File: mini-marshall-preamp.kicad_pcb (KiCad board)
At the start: 2 copper layers, 44 parts, among them J1 LO, J2 HI, J3 AudioJack2, J4 6V3, J5 370V GND, J6 370V, J7 6V3 GND, U1 6N2P, U2 6N2P

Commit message: Use external connection footprints for pots and jacks
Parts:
- J1: footprint Connector_Audio:Jack_6.35mm_Neutrik_NMJ6HFD2-AU_Horizontal -> Connector_Wire:SolderWire-1sqmm_1x04_P5.4mm_D1.4mm_OD2.7mm
- J2: footprint Connector_Audio:Jack_6.35mm_Neutrik_NMJ6HFD2-AU_Horizontal -> Connector_Wire:SolderWire-1sqmm_1x02_P5.4mm_D1.4mm_OD2.7mm
- J3: value AudioJack2 -> OUT; footprint Connector_Audio:Jack_6.35mm_Neutrik_NMJ6HFD2-AU_Horizontal -> Connector_Wire:SolderWire-1sqmm_1x02_P5.4mm_D1.4mm_OD2.7mm
- RV1, RV2, RV3, RV4, RV5: footprint Potentiometer_THT:Potentiometer_Alps_RK163_Single_Horizontal -> Connector_Wire:SolderWire-1sqmm_1x03_P5.4mm_D1.4mm_OD2.7mm
- moved C9 65.8 mm to (129.9, 118.4), turned to 90 degrees
- moved R11 58.1 mm to (116.3, 112.7), turned to 90 degrees
- moved C5 49.6 mm to (151.8, 102.1), turned to -90 degrees
- moved R4 40.8 mm to (97.7, 112.4), turned to 90 degrees
- moved J2 37.1 mm to (46.0, 102.9)
- moved J1 35.6 mm to (45.9, 85.0), turned to 90 degrees
- moved C4 26.5 mm to (94.2, 117.7), turned to 180 degrees
- moved C3 16.2 mm to (106.0, 99.8), turned to -90 degrees
- turned RV1 to 180 degrees
- turned RV2 to 180 degrees
- turned RV3 to 180 degrees
- turned RV4 to 180 degrees
- turned RV5 to 180 degrees
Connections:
- C2 pad 1: Net-(C2-Pad1) -> Net-(J1-SN)
- C3 pad 1: Net-(C3-Pad1) -> Net-(J1-S)
- R1 pad 1: Net-(J2-PadS) -> Net-(J2-S)
- R2 pad 1: Net-(J2-PadS) -> Net-(J2-S)
- R4 pad 2: Net-(C3-Pad1) -> Net-(J1-S)
- RV5 pad 2: Net-(J3-PadS) -> Net-(J3-S)

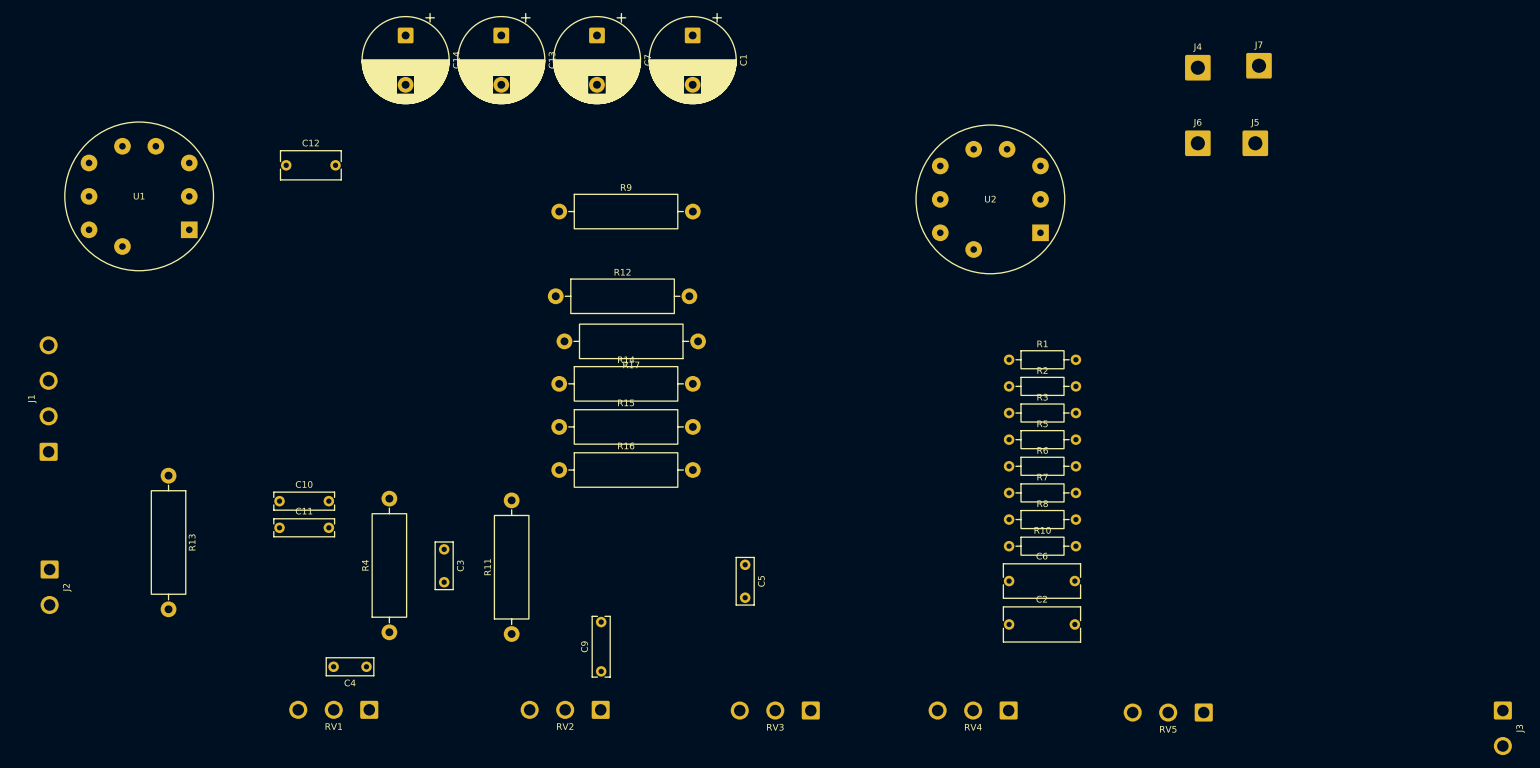
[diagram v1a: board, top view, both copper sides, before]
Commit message: First PCB layout
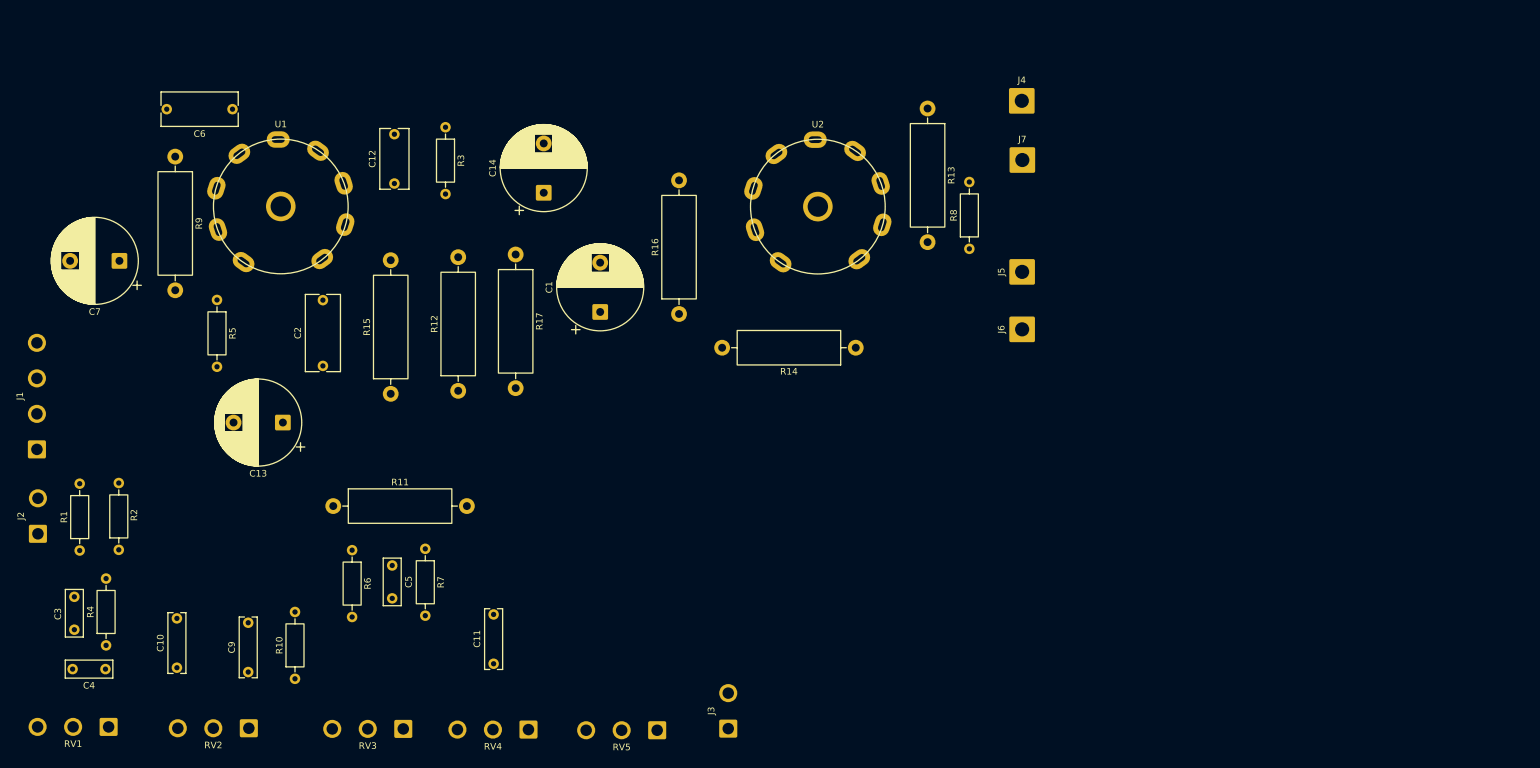
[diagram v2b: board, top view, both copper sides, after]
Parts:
- R4: footprint Resistor_THT:R_Axial_DIN0516_L15.5mm_D5.0mm_P20.32mm_Horizontal -> Resistor_THT:R_Axial_DIN0207_L6.3mm_D2.5mm_P10.16mm_Horizontal
- U1, U2: footprint Valve:Valve_Noval_P -> tubes:Valve_6N2P-3
- moved R1 144.3 mm to (50.6, 100.0), turned to 90 degrees
- moved C6 138.2 mm to (73.8, 32.9), turned to 180 degrees
- moved R2 137.6 mm to (56.5, 99.9), turned to 90 degrees
- moved R13 128.2 mm to (179.5, 32.8)
- moved R5 122.3 mm to (71.5, 61.9), turned to -90 degrees
- moved J3 117.8 mm to (149.2, 127.1), turned to 90 degrees
- moved C2 111.5 mm to (87.6, 71.9), turned to 90 degrees
- moved R10 110.4 mm to (83.3, 119.5), turned to 90 degrees
- moved R6 100.7 mm to (92.0, 99.9), turned to -90 degrees
- moved R3 96.1 mm to (106.2, 35.6), turned to -90 degrees
- moved R7 89.2 mm to (103.1, 99.7), turned to -90 degrees
- moved RV5 83.2 mm to (138.4, 127.3)
- moved C7 80.3 mm to (56.6, 55.9), turned to 180 degrees
- moved RV4 73.1 mm to (118.8, 127.2)
- moved C13 67.6 mm to (81.5, 80.5), turned to 180 degrees
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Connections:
- J2 pad 2: Net-(J2-S) -> GND

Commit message: Layout attempt
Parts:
- moved J7 80.2 mm to (115.2, 25.2)
- moved J4 78.6 mm to (115.3, 33.3)
- moved RV1 62.2 mm to (94.3, 78.6), turned to 90 degrees
- moved R2 56.0 mm to (45.7, 44.9), turned to 0 degrees
- moved C4 56.0 mm to (83.9, 70.3), turned to 0 degrees
- moved C7 55.3 mm to (109.5, 72.4), turned to -90 degrees
- moved R3 55.1 mm to (65.1, 72.3), turned to 0 degrees
- moved C6 54.1 mm to (78.2, 86.8), turned to 90 degrees
- moved R8 53.9 mm to (138.6, 80.1)
- moved J5 50.6 mm to (166.1, 99.9)
- moved R4 49.9 mm to (83.8, 73.9), turned to -90 degrees
- moved C10 48.6 mm to (112.7, 106.8)
- moved R9 47.2 mm to (107.5, 60.9), turned to 90 degrees
- moved R1 47.0 mm to (48.6, 53.0), turned to -90 degrees
- moved C3 46.6 mm to (88.6, 81.3), turned to 90 degrees
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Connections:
- C12 pad 1: Net-(U1B-K) -> Net-(U1A-K)
- C14 pad 1: Net-(U2A-A) -> Net-(U2B-A)
- C2 pad 2: Net-(U1B-A) -> Net-(U1A-A)
- C4 pad 2: Net-(U1A-G) -> Net-(U1B-G)
- C5 pad 1: Net-(U2B-G) -> Net-(U2A-G)
- C6 pad 2: Net-(U1A-A) -> Net-(U1B-A)
- C9 pad 2: Net-(U2A-K) -> Net-(U2B-K)
- J7 pad 1: GND -> GND1
- R10 pad 2: Net-(U2A-K) -> Net-(U2B-K)
- R11 pad 1: Net-(U2A-K) -> Net-(U2B-K)
- R13 pad 1: Net-(U2A-A) -> Net-(U2B-A)
- R14 pad 1: Net-(U2A-G) -> Net-(U2A-A)
- R15 pad 2: Net-(U1B-A) -> Net-(U1A-A)
- R16 pad 2: Net-(U2A-A) -> Net-(U2B-A)
- R2 pad 2: Net-(U1B-G) -> Net-(U1A-G)
- R3 pad 2: Net-(U1B-K) -> Net-(U1A-K)
- R5 pad 1: Net-(U1A-K) -> Net-(U1B-K)
- R6 pad 1: Net-(U2B-G) -> Net-(U2A-G)
- R7 pad 1: Net-(U2B-G) -> Net-(U2A-G)
- R8 pad 2: Net-(U2B-K) -> Net-(U2A-K)
- R9 pad 1: Net-(U1A-A) -> Net-(U1B-A)
- RV1 pad 2: Net-(U1A-G) -> Net-(U1B-G)
- U1 pad 5: GND -> GND1
- U2 pad 1: Net-(U2A-G) -> Net-(U2B-A)
- U2 pad 2: Net-(U2B-G) -> Net-(U2A-A)
- U2 pad 5: GND -> GND1
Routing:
- net GND: track 0.00 -> 400.0 mm
- net Net-(U2B-K): track 0.00 -> 135.2 mm
- net Net-(U2A-G): track 0.00 -> 108.0 mm
- net GND1: track 0.00 -> 80.5 mm
- net Net-(J4-Pin_1): track 0.00 -> 74.6 mm
- net Net-(RV2-Pad2): track 0.00 -> 59.1 mm
- net Net-(U1A-A): track 0.00 -> 59.0 mm
- net Net-(C7-Pad1): track 0.00 -> 54.1 mm
- net Net-(U2A-A): track 0.00 -> 50.2 mm
- net Net-(J1-S): track 0.00 -> 49.8 mm
- net Net-(U1B-A): track 0.00 -> 47.1 mm
- net Net-(C1-Pad1): track 0.00 -> 46.9 mm
- net Net-(U2B-A): track 0.00 -> 31.0 mm
- net Net-(U1A-K): track 0.00 -> 29.9 mm
- net Net-(U1B-G): track 0.00 -> 27.3 mm
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
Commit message: Layout attempt
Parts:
- moved R9 19.5 mm to (107.1, 41.5), turned to -90 degrees
- moved R10 9.21 mm to (81.8, 105.4), turned to 0 degrees
- moved C5 9.10 mm to (83.0, 95.7)
- moved R3 7.34 mm to (71.6, 68.7), turned to 90 degrees
- moved RV2 6.91 mm to (107.0, 112.3), turned to 90 degrees
- moved R7 6.89 mm to (88.2, 90.9)
- turned R6 to 180 degrees
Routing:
- net GND: track 400.0 -> 325.8 mm
- net Net-(C7-Pad1): track 54.1 -> 31.3 mm
- net Net-(U1B-A): track 47.1 -> 61.9 mm
- net Net-(U2A-G): track 108.0 -> 120.2 mm
- net Net-(C1-Pad1): track 46.9 -> 57.8 mm
- net Net-(U2B-K): track 135.2 -> 127.3 mm
- net Net-(C10-Pad2): track 25.2 -> 32.9 mm
- net Net-(C5-Pad2): track 15.7 -> 8.98 mm
- net Net-(RV2-Pad2): track 59.1 -> 53.4 mm
- net Net-(C9-Pad1): track 8.03 -> 13.3 mm
- net Net-(U1A-K): track 29.9 -> 32.8 mm
- net Net-(C10-Pad1): track 19.3 -> 21.5 mm
- net Net-(U2A-A): track 50.2 -> 51.7 mm

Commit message: Layout attempt
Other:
- board outline added: 135 x 102.1 mm
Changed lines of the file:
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@@
 		)
+	)
+	(gr_rect
+		(start 38.4556 18.4404)
+		(end 173.4312 120.523)
+		(stroke
+			(width 0.05)
+			(type default)
+		)
+		(fill no)
+		(layer "Edge.Cuts")
 	)
 	(segment
@@
 	)
 	(segment
-		(start 60.3962 94.2644)
-		(end 70.5866 84.074)
+		(start 72.4662 84.074)
+		(end 83.82 84.074)
+		(width 2)
+		(layer "B.Cu")
+		(net 26)
+	)
+	(segment
+		(start 60.4774 94.1832)
+		(end 70.6628 83.9978)
+		(width 2)
+		(layer "B.Cu")
+		(net 26)
+	)
+	(segment
+		(start 70.6628 83.9978)
+		(end 72.39 83.9978)
+		(width 2)
+		(layer "B.Cu")
+		(net 26)
+	)
+	(segment
+		(start 55.5194 94.2644)
+		(end 55.6006 94.1832)
 		(width 2)
 		(layer "B.Cu")
@@
 	)
 	(segment
-		(start 70.5866 84.074)
-		(end 83.82 84.074)
+		(start 72.39 83.9978)
+		(end 72.4662 84.074)
+		(width 2)
+		(layer "B.Cu")
+		(net 26)
+	)
+	(segment
+		(start 44.2468 94.2644)
+		(end 55.5194 94.2644)
 		(width 2)
 		(layer "B.Cu")
@@
 	)
 	(segment
-		(start 44.2468 94.2644)
-		(end 60.3962 94.2644)
-		(width 2)
-		(layer "B.Cu")
+		(start 55.6006 94.1832)
+		(end 60.4774 94.1832)
+		(width 2)
+		(layer "B.Cu")

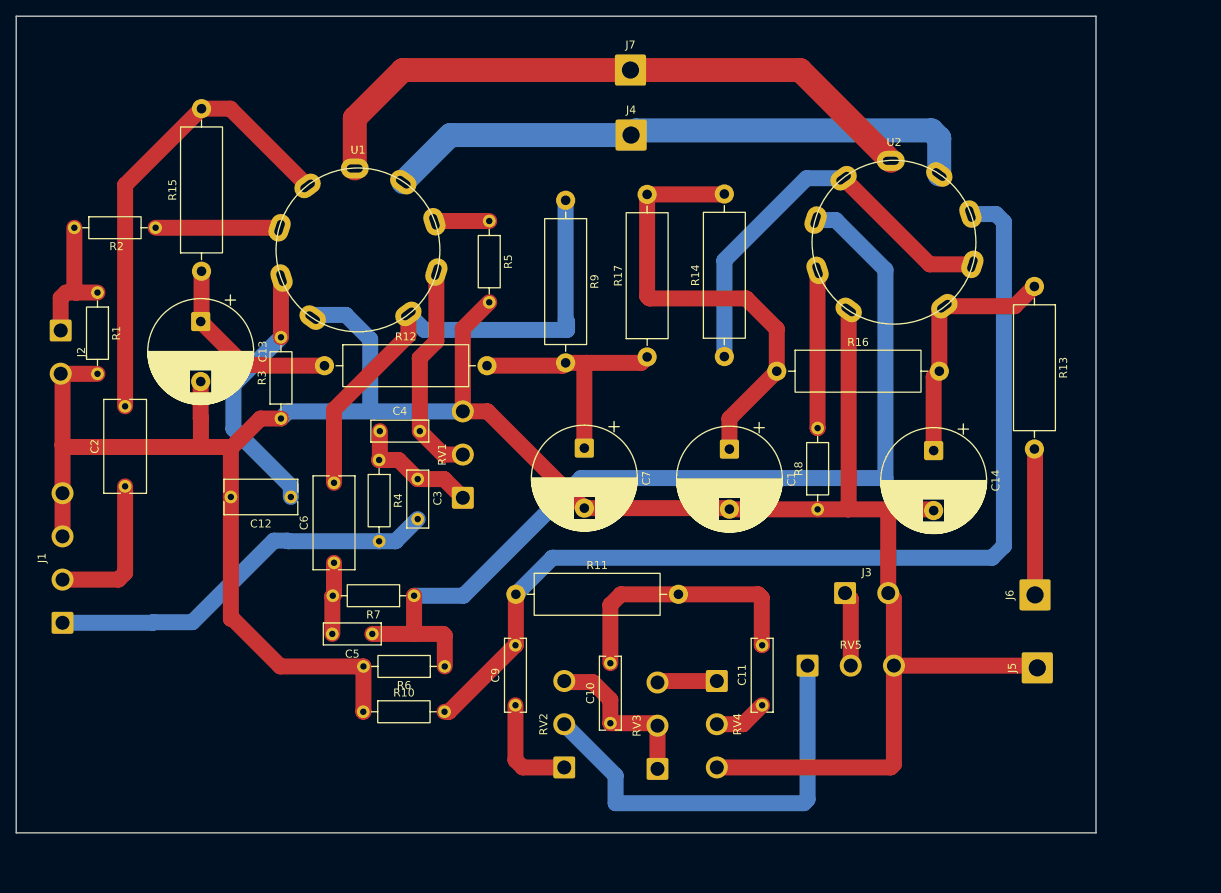
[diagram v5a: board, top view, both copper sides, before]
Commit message: Restart laying out board for size optimization
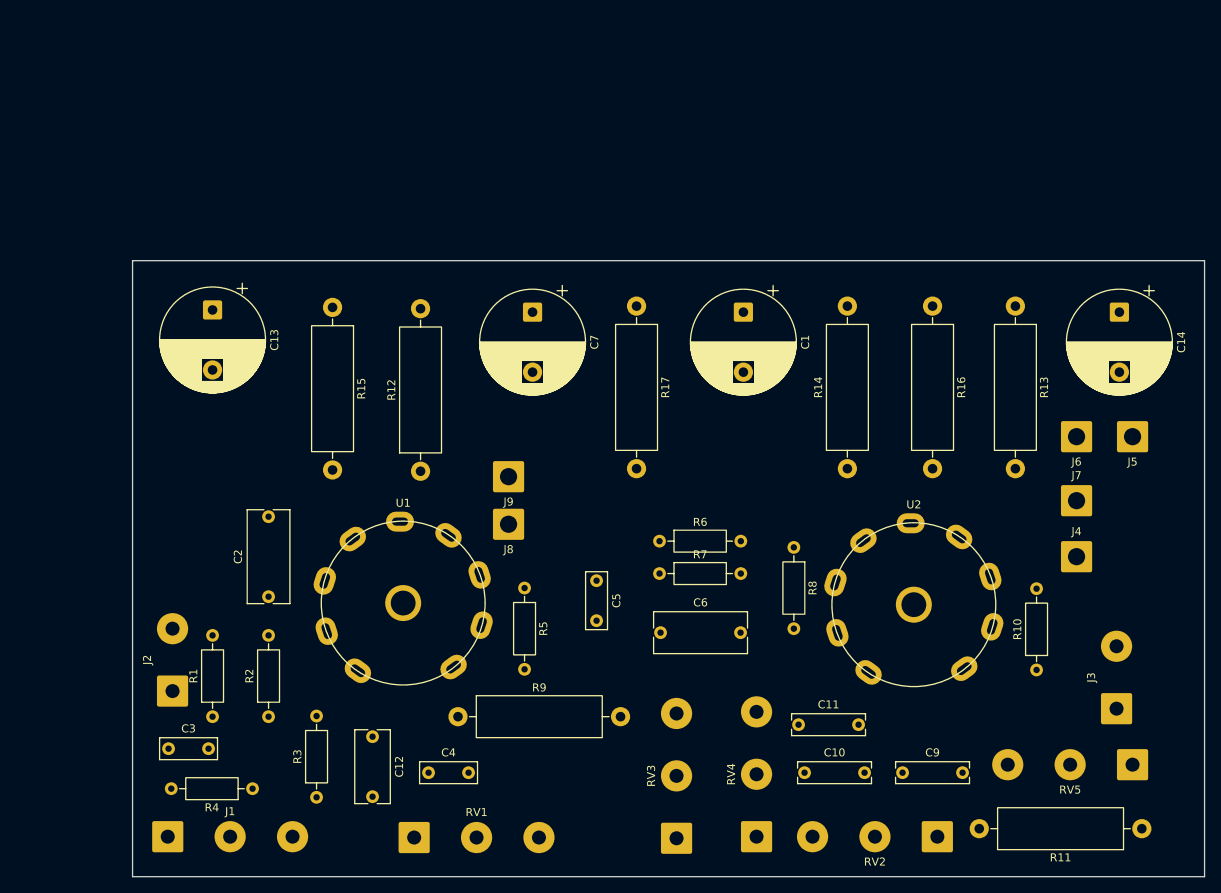
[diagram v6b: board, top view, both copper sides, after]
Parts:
- added J8: 6V3, Connector_Wire:SolderWire-1.5sqmm_1x01_D1.7mm_OD3.9mm, F.Cu at (100.0, 82.0)
- added J9: 6V3 GND, Connector_Wire:SolderWire-1.5sqmm_1x01_D1.7mm_OD3.9mm, F.Cu at (100.0, 76.0)
- J1: footprint Connector_Wire:SolderWire-1sqmm_1x04_P5.4mm_D1.4mm_OD2.7mm -> Connector_Wire:SolderWire-1sqmm_1x03_P7.8mm_D1.4mm_OD3.9mm
- J2, J3: footprint Connector_Wire:SolderWire-1sqmm_1x02_P5.4mm_D1.4mm_OD2.7mm -> Connector_Wire:SolderWire-1sqmm_1x02_P7.8mm_D1.4mm_OD3.9mm
- RV1, RV2, RV3, RV4, RV5: footprint Connector_Wire:SolderWire-1sqmm_1x03_P5.4mm_D1.4mm_OD2.7mm -> Connector_Wire:SolderWire-1sqmm_1x03_P7.8mm_D1.4mm_OD3.9mm
- moved R10 84.3 mm to (166.0, 100.2), turned to 90 degrees
- moved R11 83.6 mm to (179.2, 120.0), turned to 180 degrees
- moved J7 77.5 mm to (171.0, 79.0)
- moved J4 76.7 mm to (171.0, 86.0)
- moved R9 65.9 mm to (93.7, 106.0), turned to 0 degrees
- moved R2 65.8 mm to (70.0, 106.0), turned to 90 degrees
- moved R1 54.9 mm to (63.0, 106.0), turned to 90 degrees
- moved C9 49.1 mm to (149.2, 113.0), turned to 0 degrees
- moved R3 47.6 mm to (76.0, 116.1)
- moved RV2 47.4 mm to (153.6, 121.0), turned to 180 degrees
- moved J2 47.2 mm to (58.0, 102.8), turned to 90 degrees
- moved R5 46.1 mm to (102.0, 89.9)
- moved U2 45.4 mm to (157.0, 100.0)
- moved U1 44.5 mm to (93.1, 99.8)
- moved R4 44.0 mm to (68.0, 115.0), turned to 180 degrees
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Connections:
- net Net-(J4-Pin_1) renamed /heater
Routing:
- net GND: track 325.8 -> 0.00 mm
- net Net-(U2B-K): track 127.3 -> 0.00 mm
- net Net-(U2A-G): track 120.2 -> 0.00 mm
- net GND1: track 80.5 -> 0.00 mm
- net /heater: track 74.6 -> 0.00 mm
- net Net-(U1B-A): track 61.9 -> 0.00 mm
- net Net-(U1A-A): track 59.0 -> 0.00 mm
- net Net-(C1-Pad1): track 57.8 -> 0.00 mm
- net Net-(RV2-Pad2): track 53.4 -> 0.00 mm
- net Net-(U2A-A): track 51.7 -> 0.00 mm
- net Net-(J1-S): track 49.8 -> 0.00 mm
- net Net-(C10-Pad2): track 32.9 -> 0.00 mm
- net Net-(U1A-K): track 32.8 -> 0.00 mm
- net Net-(C7-Pad1): track 31.3 -> 0.00 mm
- net Net-(U2B-A): track 31.0 -> 0.00 mm
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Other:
- board size 135 x 102.1 mm -> 134 x 77 mm

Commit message: Nice layout
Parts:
- J1: footprint Connector_Wire:SolderWire-1sqmm_1x03_P7.8mm_D1.4mm_OD3.9mm -> Connector_Wire:SolderWire-1sqmm_1x04_P7.8mm_D1.4mm_OD3.9mm
- moved C5 6.10 mm to (114.5, 84.0)
- moved C9 3.01 mm to (149.5, 110.0)
- moved R12 2.76 mm to (86.2, 75.5)
- moved C6 2.50 mm to (116.5, 95.5), turned to 180 degrees
- moved J5 1.60 mm to (179.6, 70.9)
- moved J9 1.32 mm to (101.2, 75.3)
- moved J8 1.25 mm to (101.2, 82.5)
- moved R10 1.00 mm to (167.0, 100.1)
- moved J4 0.75 mm to (171.8, 86.0)
- moved J7 0.67 mm to (171.7, 78.8)
- moved R5 0.65 mm to (102.5, 90.3)
- moved R17 0.63 mm to (116.1, 55.3)
- moved C3 0.35 mm to (57.9, 110.0)
- moved C1 0.14 mm to (129.5, 55.3)
- moved C14 0.14 mm to (176.5, 55.3)
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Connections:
- net Net-(U2B-A) renamed /anode
- J4 pad 1: /heater -> Net-(J4-Pin_1)
- J8 pad 1: /heater -> Net-(J8-Pin_1)
- U1 pad 4: /heater -> Net-(J8-Pin_1)
- U2 pad 4: /heater -> Net-(J4-Pin_1)
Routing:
- net GND: track 0.00 -> 384.2 mm
- net Net-(C7-Pad1): track 0.00 -> 82.3 mm
- net /anode: track 0.00 -> 75.9 mm
- net Net-(U2B-K): track 0.00 -> 60.9 mm
- net Net-(C1-Pad1): track 0.00 -> 49.8 mm
- net Net-(C3-Pad2): track 0.00 -> 41.1 mm
- net Net-(U1B-G): track 0.00 -> 40.5 mm
- net GND1: track 0.00 -> 40.0 mm
- net Net-(U2A-G): track 0.00 -> 39.5 mm
- net Net-(C13-Pad1): track 0.00 -> 39.3 mm
- net Net-(RV2-Pad2): track 0.00 -> 38.8 mm
- net Net-(C10-Pad1): track 0.00 -> 32.2 mm
- net Net-(J1-SN): track 0.00 -> 32.0 mm
- net Net-(U2A-A): track 0.00 -> 30.5 mm
- net Net-(C5-Pad2): track 0.00 -> 25.9 mm
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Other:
- board size 134 x 77 mm -> 133.4 x 76.5 mm
